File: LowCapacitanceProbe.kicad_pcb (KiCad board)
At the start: 2 copper layers, 25.1 x 19.4 mm, 40 parts, among them J2 SMA, J3 Barrel_Jack_Switch, Q1 BF998, U2 SPX3819M5-L-5-0

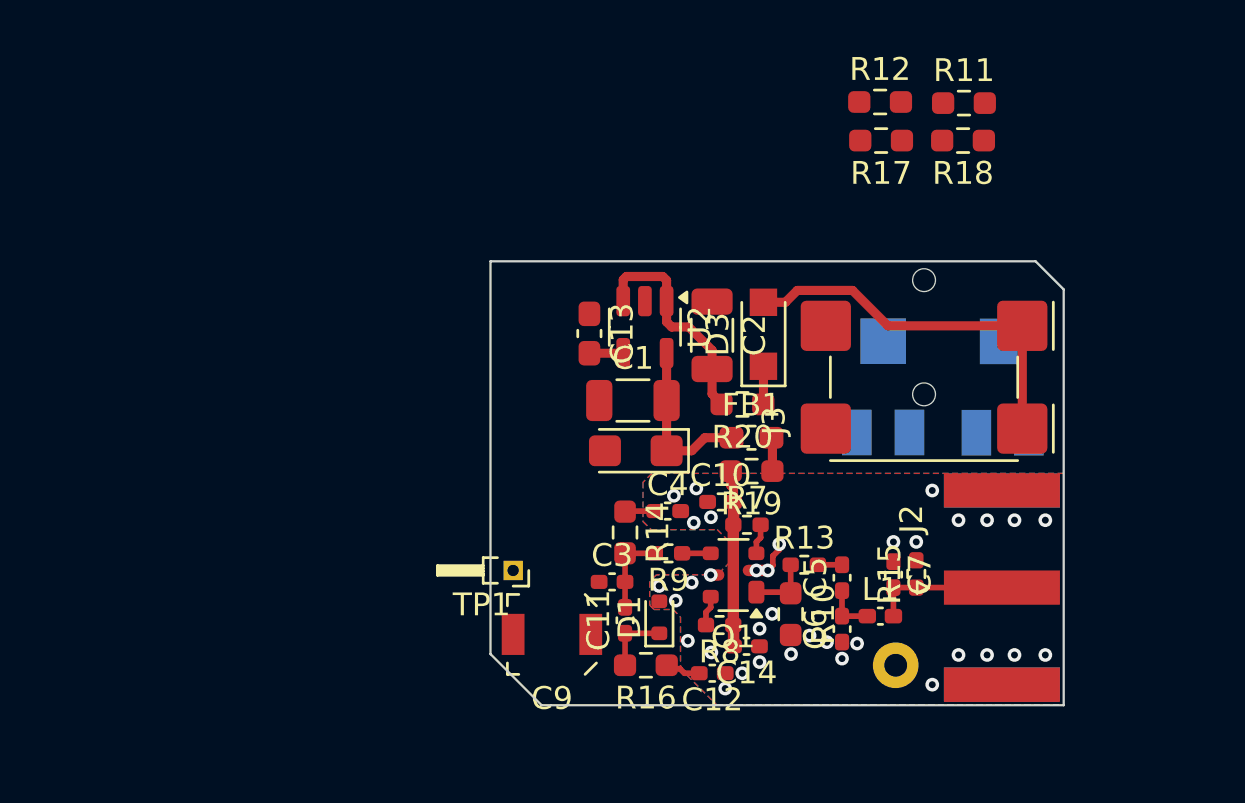
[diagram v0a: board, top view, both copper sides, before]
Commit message: Further work on routing, change to 4 layers is imminent.
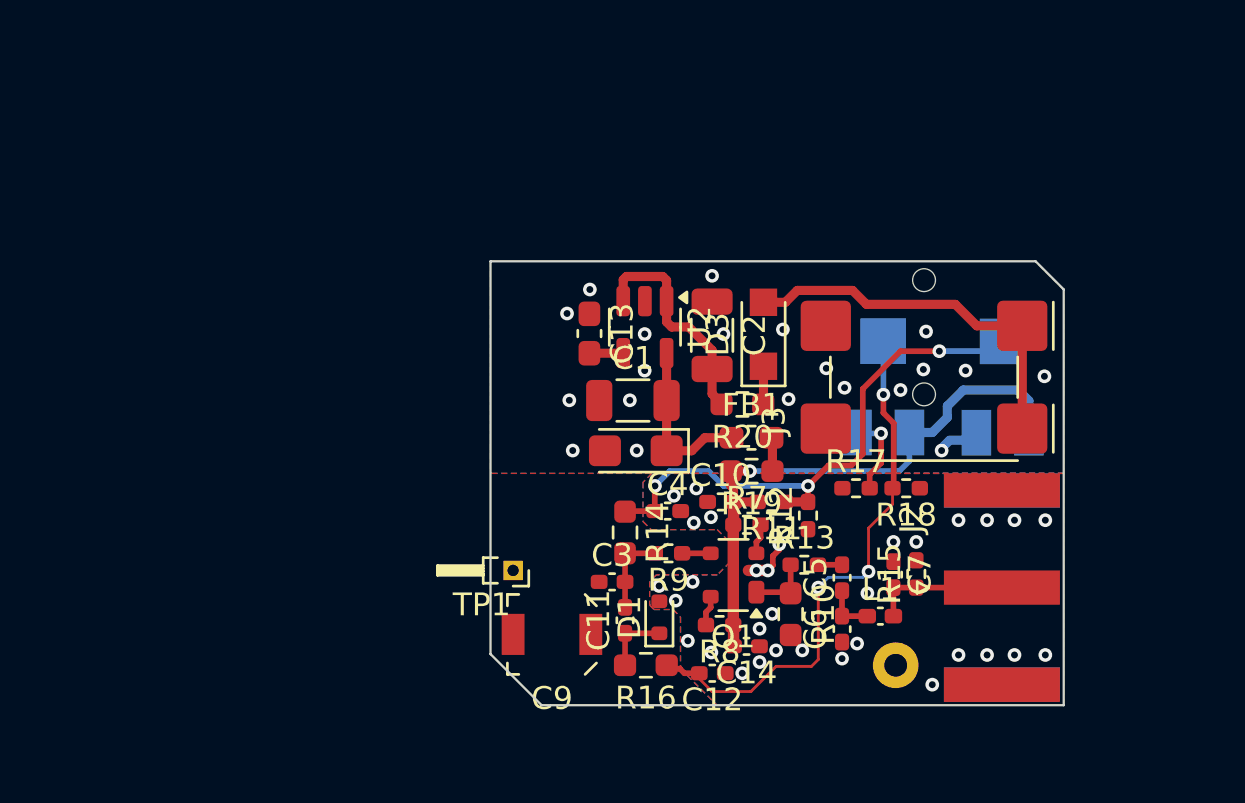
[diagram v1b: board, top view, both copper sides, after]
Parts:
- R11, R12, R17, R18: footprint Resistor_SMD:R_0603_1608Metric_Pad0.98x0.95mm_HandSolder -> Resistor_SMD:R_0402_1005Metric_Pad0.72x0.64mm_HandSolder
- moved R11 19.4 mm to (124.9, 66.5), turned to 180 degrees
- moved R12 18.4 mm to (126.5, 67.1), turned to 90 degrees
- moved R18 15.4 mm to (130.8, 65.9)
- moved R17 15.3 mm to (128.6, 65.9), turned to 0 degrees
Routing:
- net /G2_BIAS: track 1.31 -> 24.2 mm, vias 0 -> 3
- net /GAIN_TUNE: track 1.58 -> 24.2 mm, vias 0 -> 3
- net /POWER: track 7.73 -> 25.9 mm, vias 0 -> 1
- net Net-(R17-Pad2): track 0.00 -> 3.68 mm, vias 0 -> 1
- net GND: track 12.8 -> 14.3 mm, vias 35 -> 52

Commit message: More routing
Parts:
- moved R11 17.7 mm to (141.9, 61.6)
- moved R12 14.7 mm to (140.8, 63.6), turned to 180 degrees
- moved R20 4.83 mm to (123.5, 57.4)
- moved R18 3.96 mm to (126.9, 65.6), turned to 0 degrees
- moved R17 1.87 mm to (126.9, 66.5)
- moved D3 1.29 mm to (124.6, 60.5), turned to -90 degrees
- moved C2 1.25 mm to (122.3, 60.5), turned to 90 degrees
- moved R19 0.15 mm to (124.0, 65.3)
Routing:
- net /G2_BIAS: track 24.2 -> 3.01 mm, vias 3 -> 1
- net /GAIN_TUNE: track 24.2 -> 10.1 mm
- net /PIN: track 16.7 -> 4.50 mm
- net /POWER: track 25.9 -> 15.5 mm, vias 1 -> 0
- net /PIN_FILT: track 9.83 -> 3.88 mm
- net Net-(D3-K): track 1.67 -> 0.00 mm
- net Net-(R17-Pad2): track 3.68 -> 4.77 mm
- net GND: track 14.3 -> 13.5 mm
- added copper zone on In1.Cu, net GND
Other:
- copper layers 2 -> 4
- rule pad_to_mask_clearance: 0.05 -> 0

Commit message: Some more routing, modified outjob.
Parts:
- moved R11 11.9 mm to (130.8, 66.0), turned to 0 degrees
- moved R12 10.5 mm to (130.8, 67.0)
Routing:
- net /G2_BIAS: track 3.01 -> 28.8 mm, vias 1 -> 2
- net /GAIN_TUNE: track 10.1 -> 25.9 mm
- net /PIN: track 4.50 -> 17.1 mm
- net /POWER: track 15.5 -> 26.6 mm, vias 0 -> 2
- net /PIN_FILT: track 3.88 -> 8.32 mm
- net Net-(C3-Pad1): track 0.00 -> 2.70 mm
- net Net-(D3-K): track 0.00 -> 1.70 mm
- net GND: track 13.5 -> 15.0 mm, vias 52 -> 55

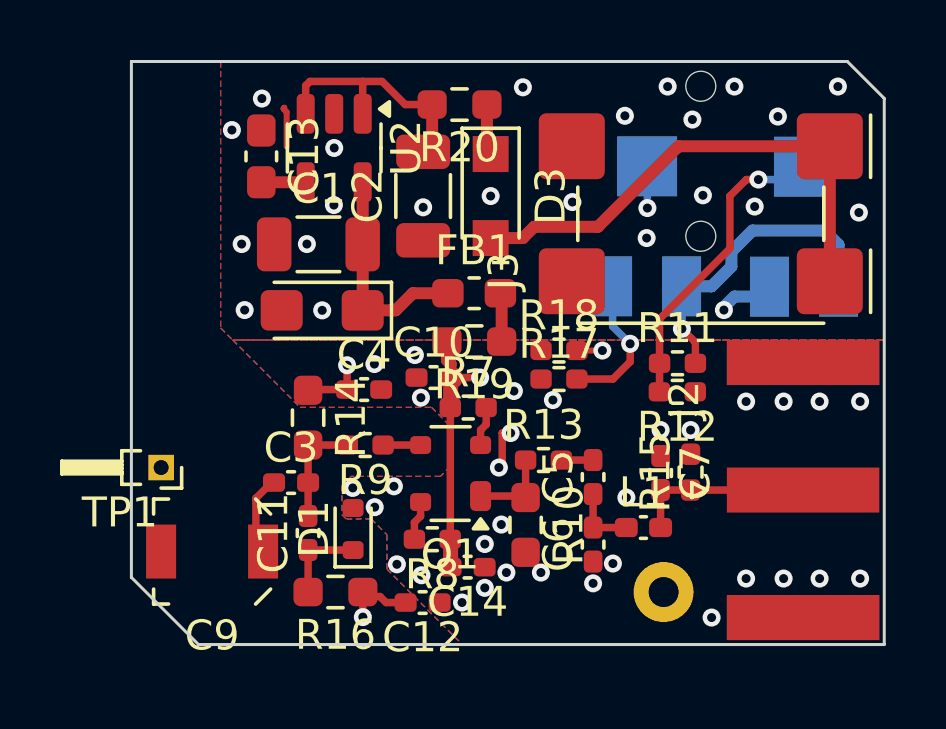
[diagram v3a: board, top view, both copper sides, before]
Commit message: Additional routing, finalizing PCB shape.
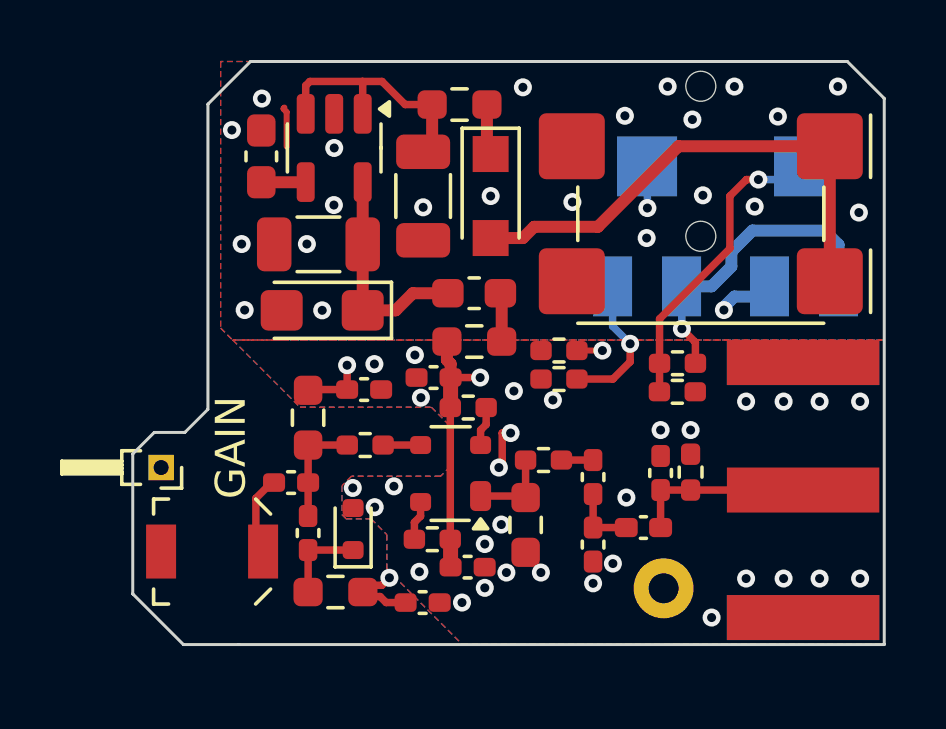
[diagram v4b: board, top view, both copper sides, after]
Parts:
- moved TP3 0.12 mm to (130.3, 73.5)
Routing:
- net /GAIN_TUNE: track 25.9 -> 23.4 mm
- net GND: track 15.0 -> 14.9 mm, vias 55 -> 54
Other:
- outline, holes or cut-outs redrawn
- board text added: "BIAS"
- board text added: "GAIN"

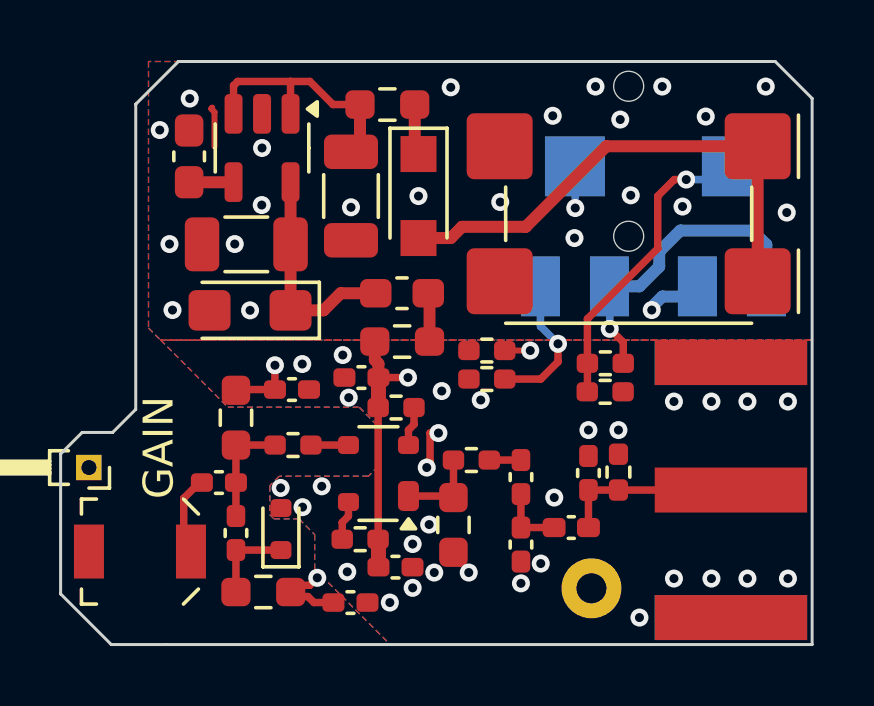
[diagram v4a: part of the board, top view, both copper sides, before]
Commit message: Started adding JLCPCB rules, board rules, net classes, component classes, custom DRC rules, finishing board, RF traces for JLCPCB 4L 3313, unmasked outline for conductive case etc.
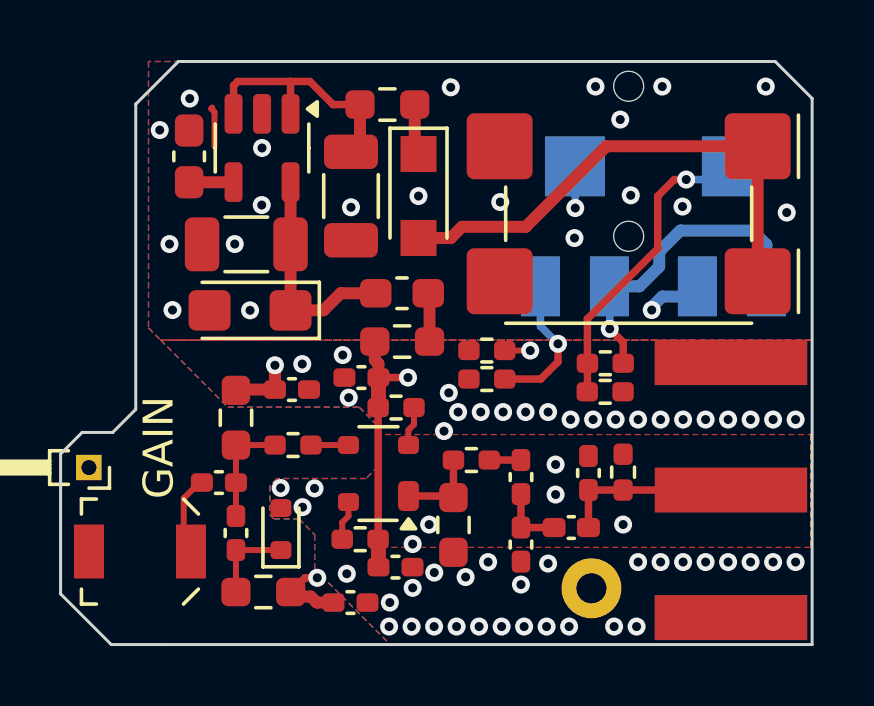
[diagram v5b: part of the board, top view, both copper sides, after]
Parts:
- moved R15 0.16 mm to (131.4, 69.7)
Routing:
- net GND: track 14.9 -> 10.3 mm, vias 54 -> 77
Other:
- rule pad_to_mask_clearance: 0 -> 0.038

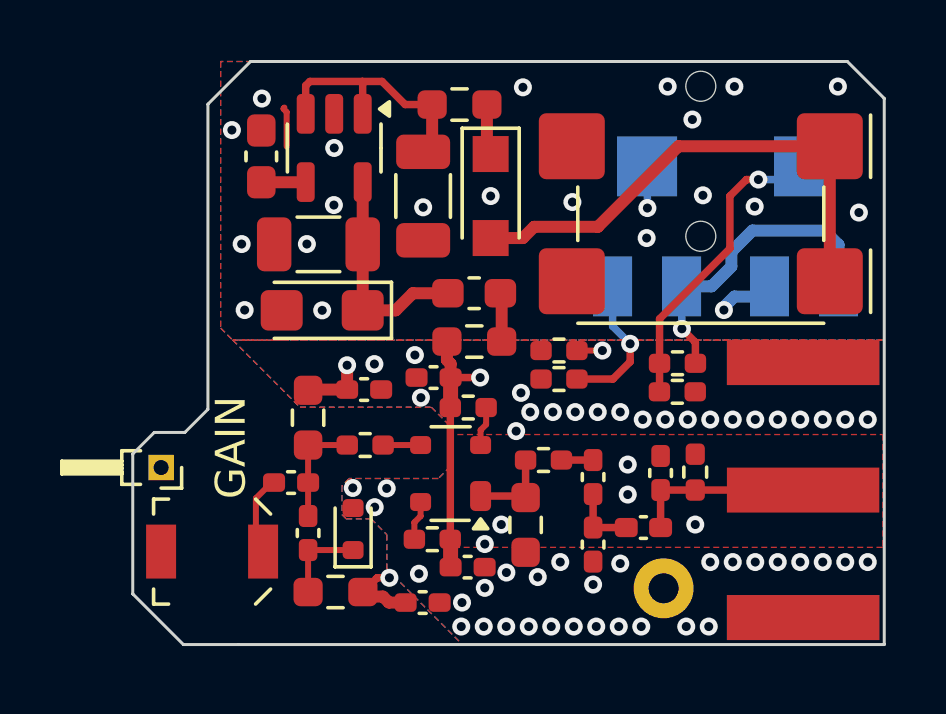
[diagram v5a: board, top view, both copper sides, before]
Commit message: Added footprint and model of P50 broken needle and whole pogo with sleeve. Finalizing shape and ground contacts.
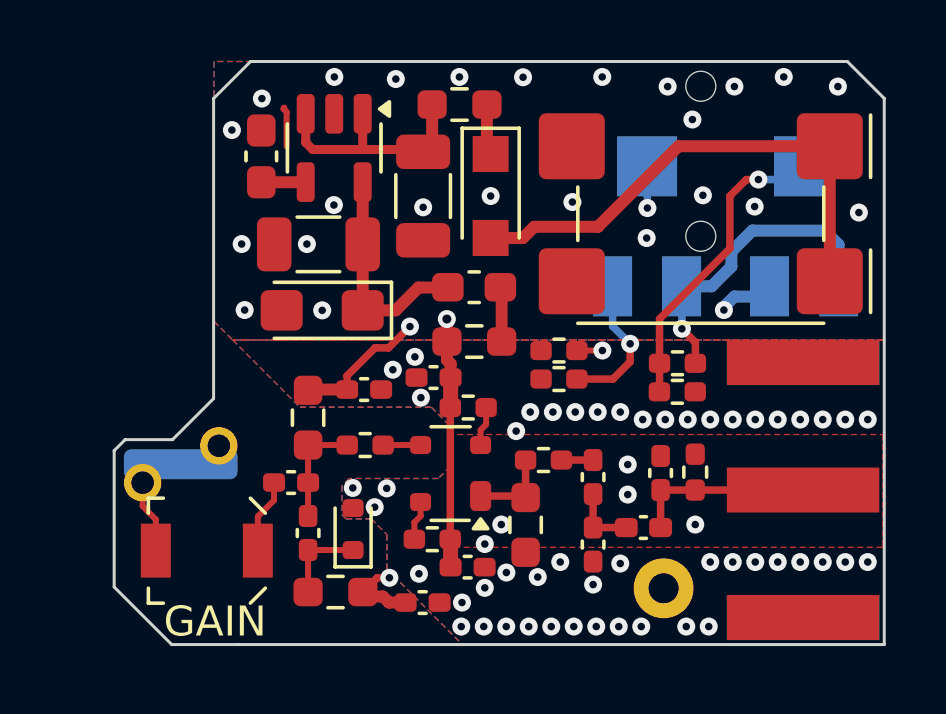
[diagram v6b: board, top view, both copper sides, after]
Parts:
- TP1: footprint Connector_PinHeader_1.00mm:PinHeader_1x01_P1.00mm_Horizontal -> petr:P50-B1_needle; moved to B.Cu
- moved TP1 0.62 mm to (113.0, 69.4)
- moved FB1 0.20 mm to (124.0, 63.5)
- moved C9 0.18 mm to (115.1, 72.3)
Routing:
- net /GAIN_TUNE: track 23.4 -> 27.1 mm
- net /IN: track 0.00 -> 2.45 mm
- net /POWER: track 26.6 -> 28.2 mm
- net /G2_BIAS: track 28.8 -> 29.5 mm
- net GND: vias 77 -> 80
- added copper zone on In2.Cu, net GND
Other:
- board size 25.1 x 19.4 mm -> 25.7 x 19.4 mm

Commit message: Some macdinking, review/checklist in progress.
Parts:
- moved C9 19.0 mm to (96.3, 74.7)
- moved C10 19.0 mm to (103.8, 68.7)
- moved C3 19.0 mm to (99.1, 72.2)
- moved C4 19.0 mm to (101.5, 69.1)
- moved J3 19.0 mm to (112.7, 62.2)
- moved L1 19.0 mm to (110.8, 73.7)
- moved R12 19.0 mm to (112.0, 69.2)
- moved R19 19.0 mm to (105.2, 67.5)
- moved R7 19.0 mm to (105.0, 69.7)
- moved R9 19.0 mm to (101.6, 71.0)
- moved RV2 19.0 mm to (111.0, 63.7)
- moved U2 19.0 mm to (100.5, 61.1)
- moved C1 19.0 mm to (100.0, 64.3)
- moved C11 19.0 mm to (99.7, 73.9)
- moved C12 19.0 mm to (103.5, 76.2)
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
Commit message: Final finishing touches, checking.
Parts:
- added SYM3: SYM_ESD_Large, Symbol:ESD-Logo_6.6x6mm_SilkScreen, B.Cu at (107.3, 73.6)
- J2: value SMA -> OUTPUT
- J3: value Barrel_Jack_Switch -> POWER IN
- moved R15 0.18 mm to (112.4, 71.9)
- moved TP1 0.05 mm to (94.1, 71.6)
- moved J3 0.05 mm to (112.7, 62.1)
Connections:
- net +5V renamed /+5V
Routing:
- net GND: track 10.3 -> 8.92 mm, vias 80 -> 77
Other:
- outline, holes or cut-outs redrawn
- board text added: "${Author}"
- board text added: "${DATE}"
- board text added: "AC Low Capacitance Probe ${Version}"
